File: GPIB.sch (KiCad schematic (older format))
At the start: 12 parts

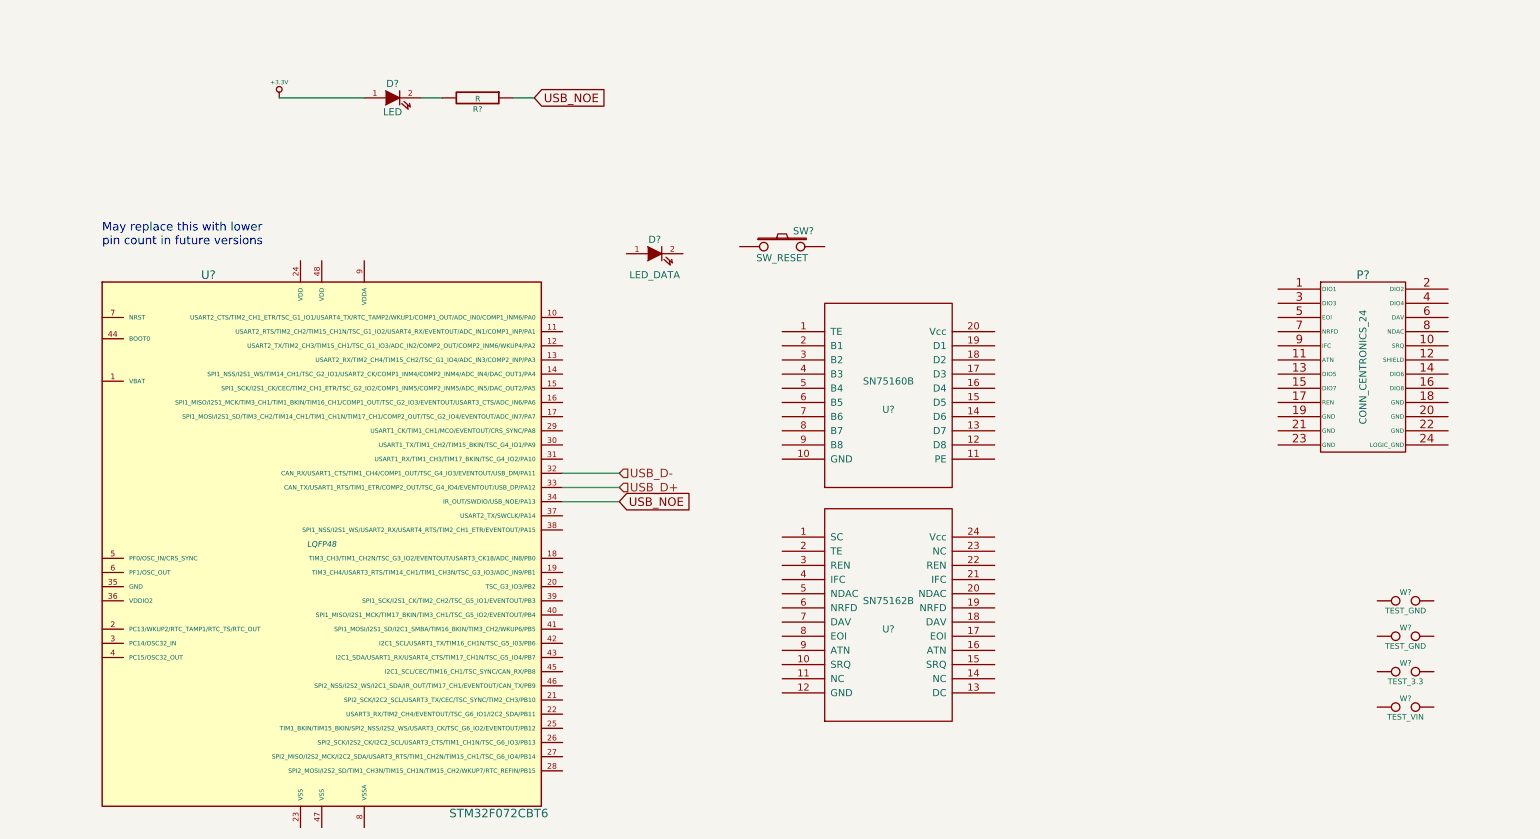
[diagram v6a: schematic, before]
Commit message: Wired up GPIB bus side
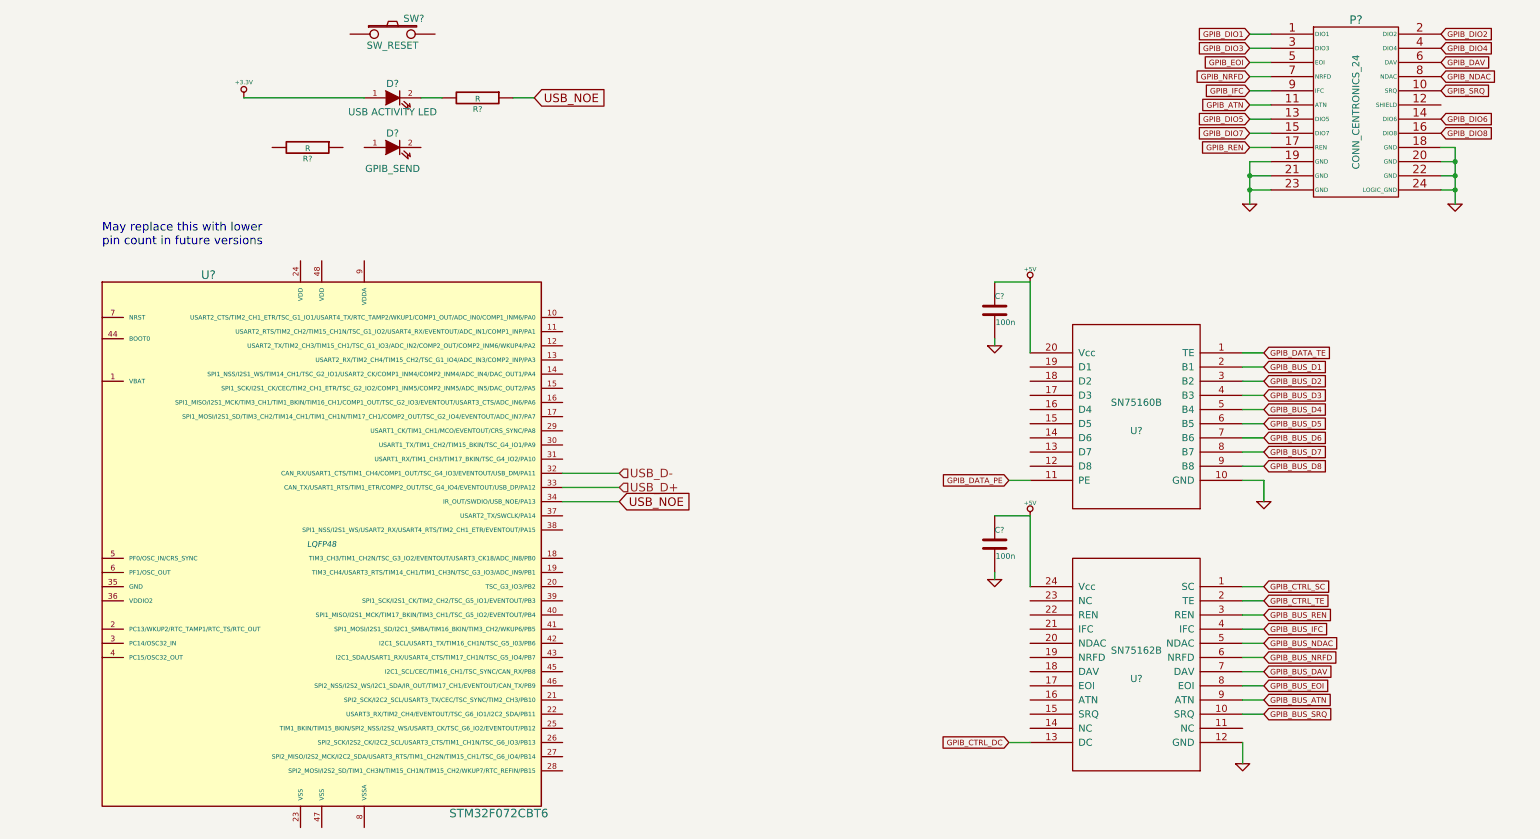
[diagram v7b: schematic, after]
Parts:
- removed W? (x2): TEST_GND, symbol TEST
- removed W?: TEST_3.3, symbol TEST
- removed W?: TEST_VIN, symbol TEST
- added C? (x2): 100n, symbol C
- added R?: R, symbol R
- D?: value LED_DATA -> GPIB_SEND
- D?: value LED -> USB ACTIVITY LED
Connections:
- net GPIB_DATA_TE: now reaches U?.1 (TE)
- net GND: now reaches U?.10 (GND)
- net GND: now also P?.18 (GND), P?.19 (GND), P?.20 (GND), P?.21 (GND), P?.22 (GND), P?.23 (GND), P?.24 (LOGIC_GND), U?.12 (GND), C?.2, C?.2
- net GPIB_DATA_PE: now reaches U?.11 (PE)
- net GPIB_BUS_D1: now reaches U?.2 (B1)
- net +5V: now reaches U?.20 (Vcc)
- net +5V: now also U?.24 (Vcc), C?.1, C?.1
- net GPIB_BUS_D2: now reaches U?.3 (B2)
- net GPIB_BUS_D3: now reaches U?.4 (B3)
- net GPIB_BUS_D4: now reaches U?.5 (B4)
- net GPIB_BUS_D5: now reaches U?.6 (B5)
- net GPIB_BUS_D6: now reaches U?.7 (B6)
- net GPIB_BUS_D7: now reaches U?.8 (B7)
- net GPIB_BUS_D8: now reaches U?.9 (B8)
- net GPIB_CTRL_SC: now reaches U?.1 (SC)
- net GPIB_BUS_SRQ: now reaches U?.10 (SRQ)
- net GPIB_CTRL_DC: now reaches U?.13 (DC)
- net GPIB_CTRL_TE: now reaches U?.2 (TE)
- net GPIB_BUS_REN: now reaches U?.3 (REN)
- net GPIB_BUS_IFC: now reaches U?.4 (IFC)
- net GPIB_BUS_NDAC: now reaches U?.5 (NDAC)
- net GPIB_BUS_NRFD: now reaches U?.6 (NRFD)
- net GPIB_BUS_DAV: now reaches U?.7 (DAV)
- net GPIB_BUS_EOI: now reaches U?.8 (EOI)
- net GPIB_BUS_ATN: now reaches U?.9 (ATN)
- net GPIB_DIO1: now reaches P?.1 (DIO1)
- net GPIB_SRQ: now reaches P?.10 (SRQ)
- net GPIB_ATN: now reaches P?.11 (ATN)
- net GPIB_DIO5: now reaches P?.13 (DIO5)
- net GPIB_DIO6: now reaches P?.14 (DIO6)
- net GPIB_DIO7: now reaches P?.15 (DIO7)
- net GPIB_DIO8: now reaches P?.16 (DIO8)
- net GPIB_REN: now reaches P?.17 (REN)
- net GPIB_DIO2: now reaches P?.2 (DIO2)
- net GPIB_DIO3: now reaches P?.3 (DIO3)
- net GPIB_DIO4: now reaches P?.4 (DIO4)
- net GPIB_EOI: now reaches P?.5 (EOI)
- net GPIB_DAV: now reaches P?.6 (DAV)
- net GPIB_NRFD: now reaches P?.7 (NRFD)
- net GPIB_NDAC: now reaches P?.8 (NDAC)
- net GPIB_IFC: now reaches P?.9 (IFC)
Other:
- moved on the sheet: D?, P?, SW?, U?

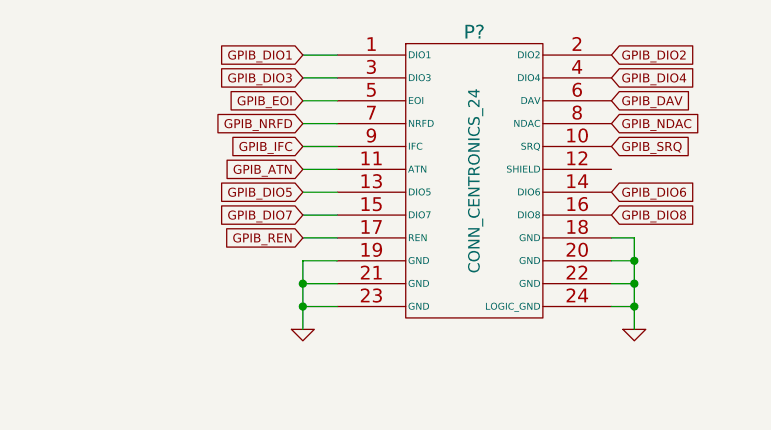
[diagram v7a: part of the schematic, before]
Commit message: Fix up GPIB port labels
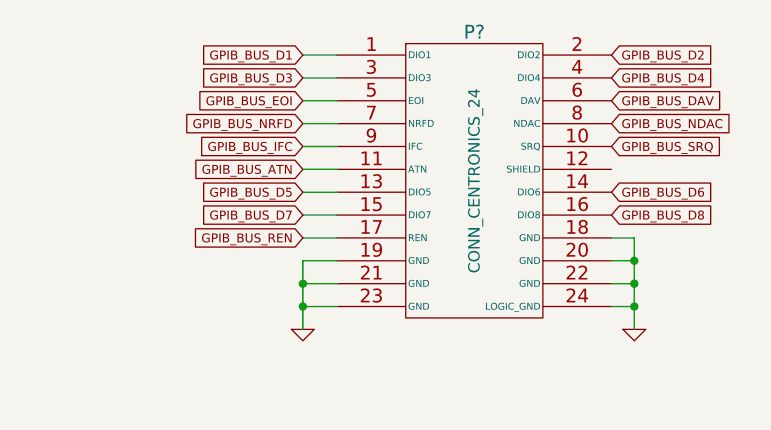
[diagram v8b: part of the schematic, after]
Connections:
- net GPIB_ATN is gone; now on net GPIB_BUS_ATN: P?.11 (ATN)
- net GPIB_DAV is gone; now on net GPIB_BUS_DAV: P?.6 (DAV)
- net GPIB_DIO1 is gone; now on net GPIB_BUS_D1: P?.1 (DIO1)
- net GPIB_DIO2 is gone; now on net GPIB_BUS_D2: P?.2 (DIO2)
- net GPIB_DIO3 is gone; now on net GPIB_BUS_D3: P?.3 (DIO3)
- net GPIB_DIO4 is gone; now on net GPIB_BUS_D4: P?.4 (DIO4)
- net GPIB_DIO5 is gone; now on net GPIB_BUS_D5: P?.13 (DIO5)
- net GPIB_DIO6 is gone; now on net GPIB_BUS_D6: P?.14 (DIO6)
- net GPIB_DIO7 is gone; now on net GPIB_BUS_D7: P?.15 (DIO7)
- net GPIB_DIO8 is gone; now on net GPIB_BUS_D8: P?.16 (DIO8)
- net GPIB_EOI is gone; now on net GPIB_BUS_EOI: P?.5 (EOI)
- net GPIB_IFC is gone; now on net GPIB_BUS_IFC: P?.9 (IFC)
- net GPIB_NDAC is gone; now on net GPIB_BUS_NDAC: P?.8 (NDAC)
- net GPIB_NRFD is gone; now on net GPIB_BUS_NRFD: P?.7 (NRFD)
- net GPIB_REN is gone; now on net GPIB_BUS_REN: P?.17 (REN)
- net GPIB_SRQ is gone; now on net GPIB_BUS_SRQ: P?.10 (SRQ)
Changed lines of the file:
@@
 	9300 1850 9450 1850
 Text GLabel 9300 750  0    39   Input ~ 0
-GPIB_DIO1
+GPIB_BUS_D1
 Text GLabel 9300 850  0    39   Input ~ 0
-GPIB_DIO3
+GPIB_BUS_D3
 Text GLabel 9300 1350 0    39   Input ~ 0
-GPIB_DIO5
+GPIB_BUS_D5
 Text GLabel 9300 1450 0    39   Input ~ 0
-GPIB_DIO7
+GPIB_BUS_D7
 Text GLabel 10650 1450 2    39   Input ~ 0
-GPIB_DIO8
+GPIB_BUS_D8
 Text GLabel 10650 1350 2    39   Input ~ 0
-GPIB_DIO6
+GPIB_BUS_D6
 Text GLabel 10650 850  2    39   Input ~ 0
-GPIB_DIO4
+GPIB_BUS_D4
 Text GLabel 10650 750  2    39   Input ~ 0
-GPIB_DIO2
+GPIB_BUS_D2
 Wire Wire Line
 	10650 1550 10750 1550
@@
 GPIB_CTRL_DC
 Text GLabel 9300 1550 0    39   Input ~ 0
-GPIB_REN
+GPIB_BUS_REN
 Text GLabel 9300 1150 0    39   Input ~ 0
-GPIB_IFC
+GPIB_BUS_IFC
 Text GLabel 10650 1050 2    39   Input ~ 0
-GPIB_NDAC
+GPIB_BUS_NDAC
 Text GLabel 9300 1050 0    39   Input ~ 0
-GPIB_NRFD
+GPIB_BUS_NRFD
 Text GLabel 10650 950  2    39   Input ~ 0
-GPIB_DAV
+GPIB_BUS_DAV
 Text GLabel 9300 950  0    39   Input ~ 0
-GPIB_EOI
+GPIB_BUS_EOI
 Text GLabel 9300 1250 0    39   Input ~ 0
-GPIB_ATN
+GPIB_BUS_ATN
 Text GLabel 10650 1150 2    39   Input ~ 0
-GPIB_SRQ
+GPIB_BUS_SRQ
 Text GLabel 9400 3000 2    39   Input ~ 0
 GPIB_DATA_TE
